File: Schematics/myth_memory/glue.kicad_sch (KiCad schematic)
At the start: 6 parts, among them U1 74HC04, U12 74LS32, U4 74LS32, U5 74LS21, U6 4002, U8 4075

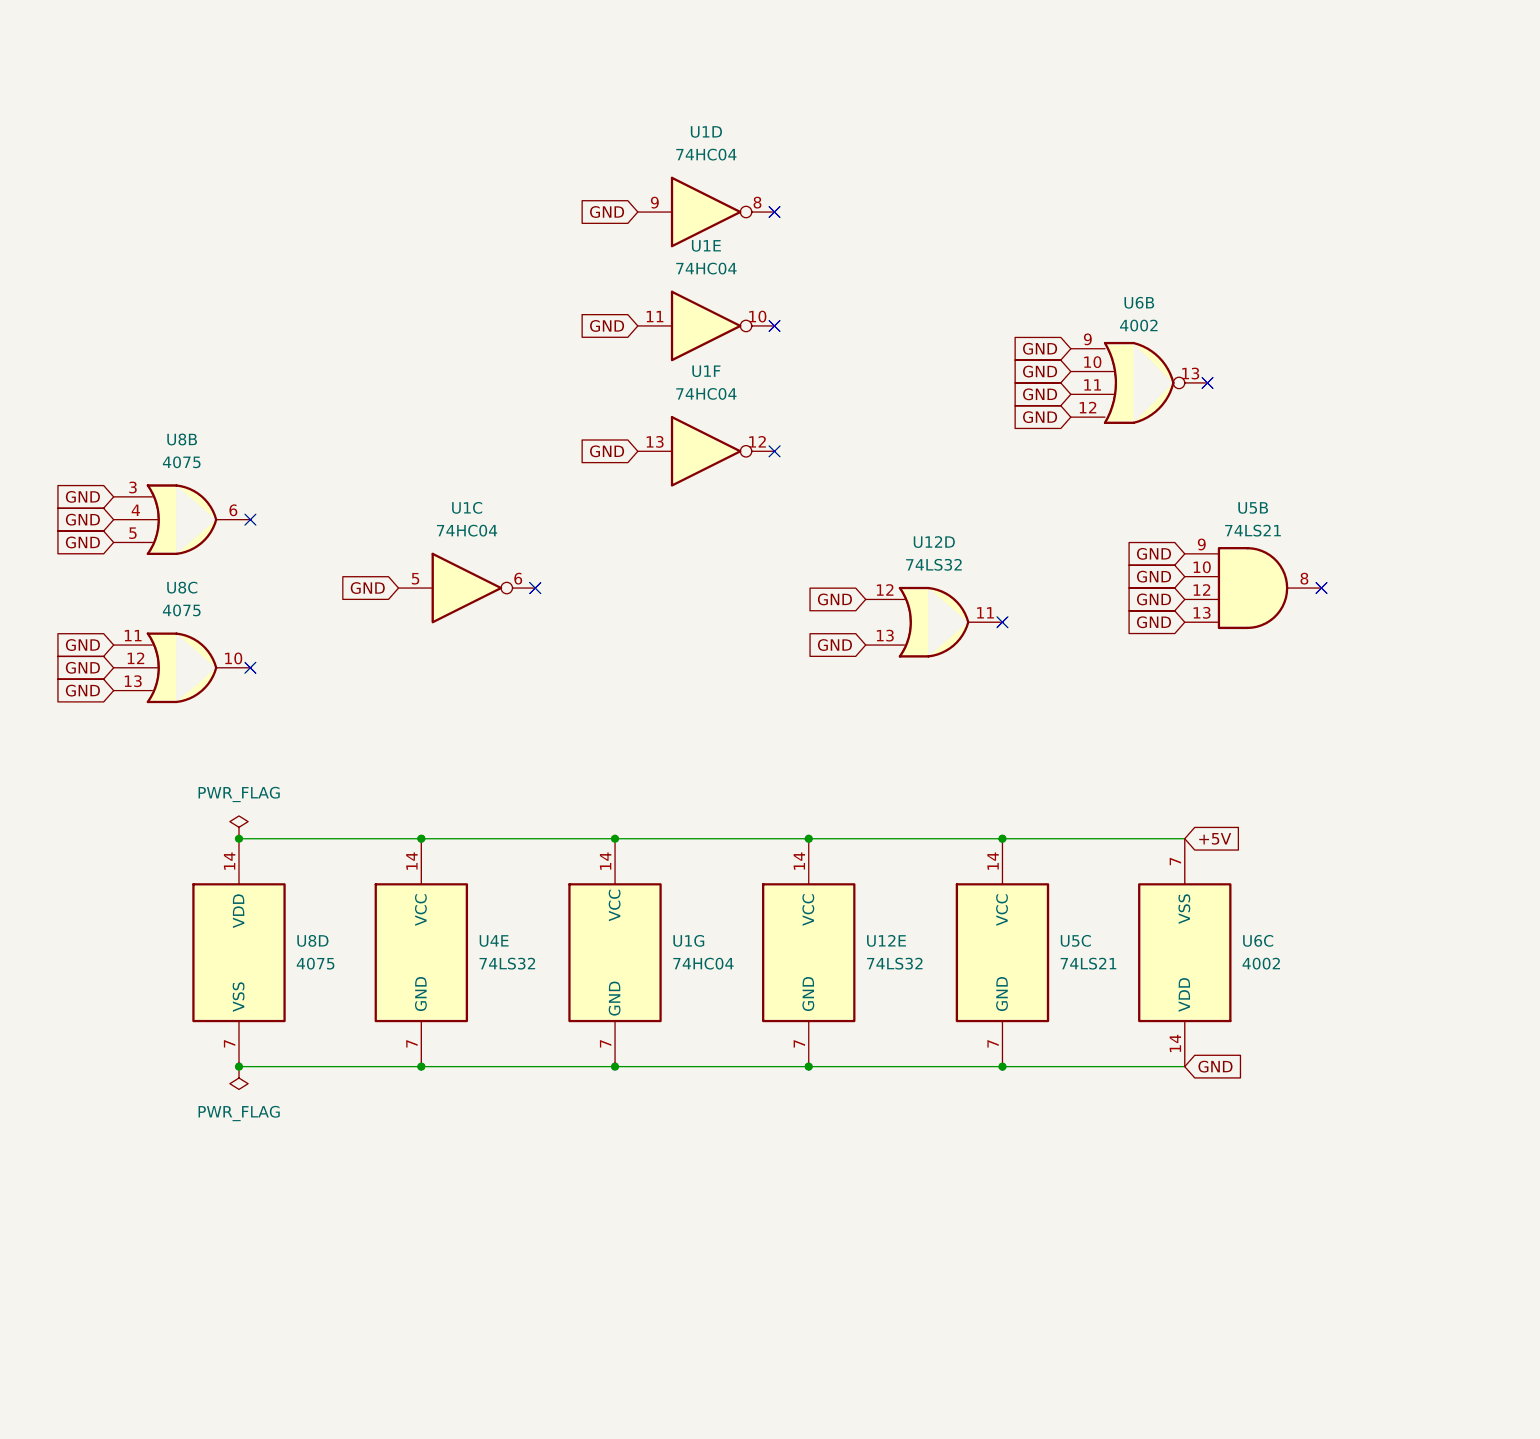
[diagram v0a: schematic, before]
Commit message: Change d to g
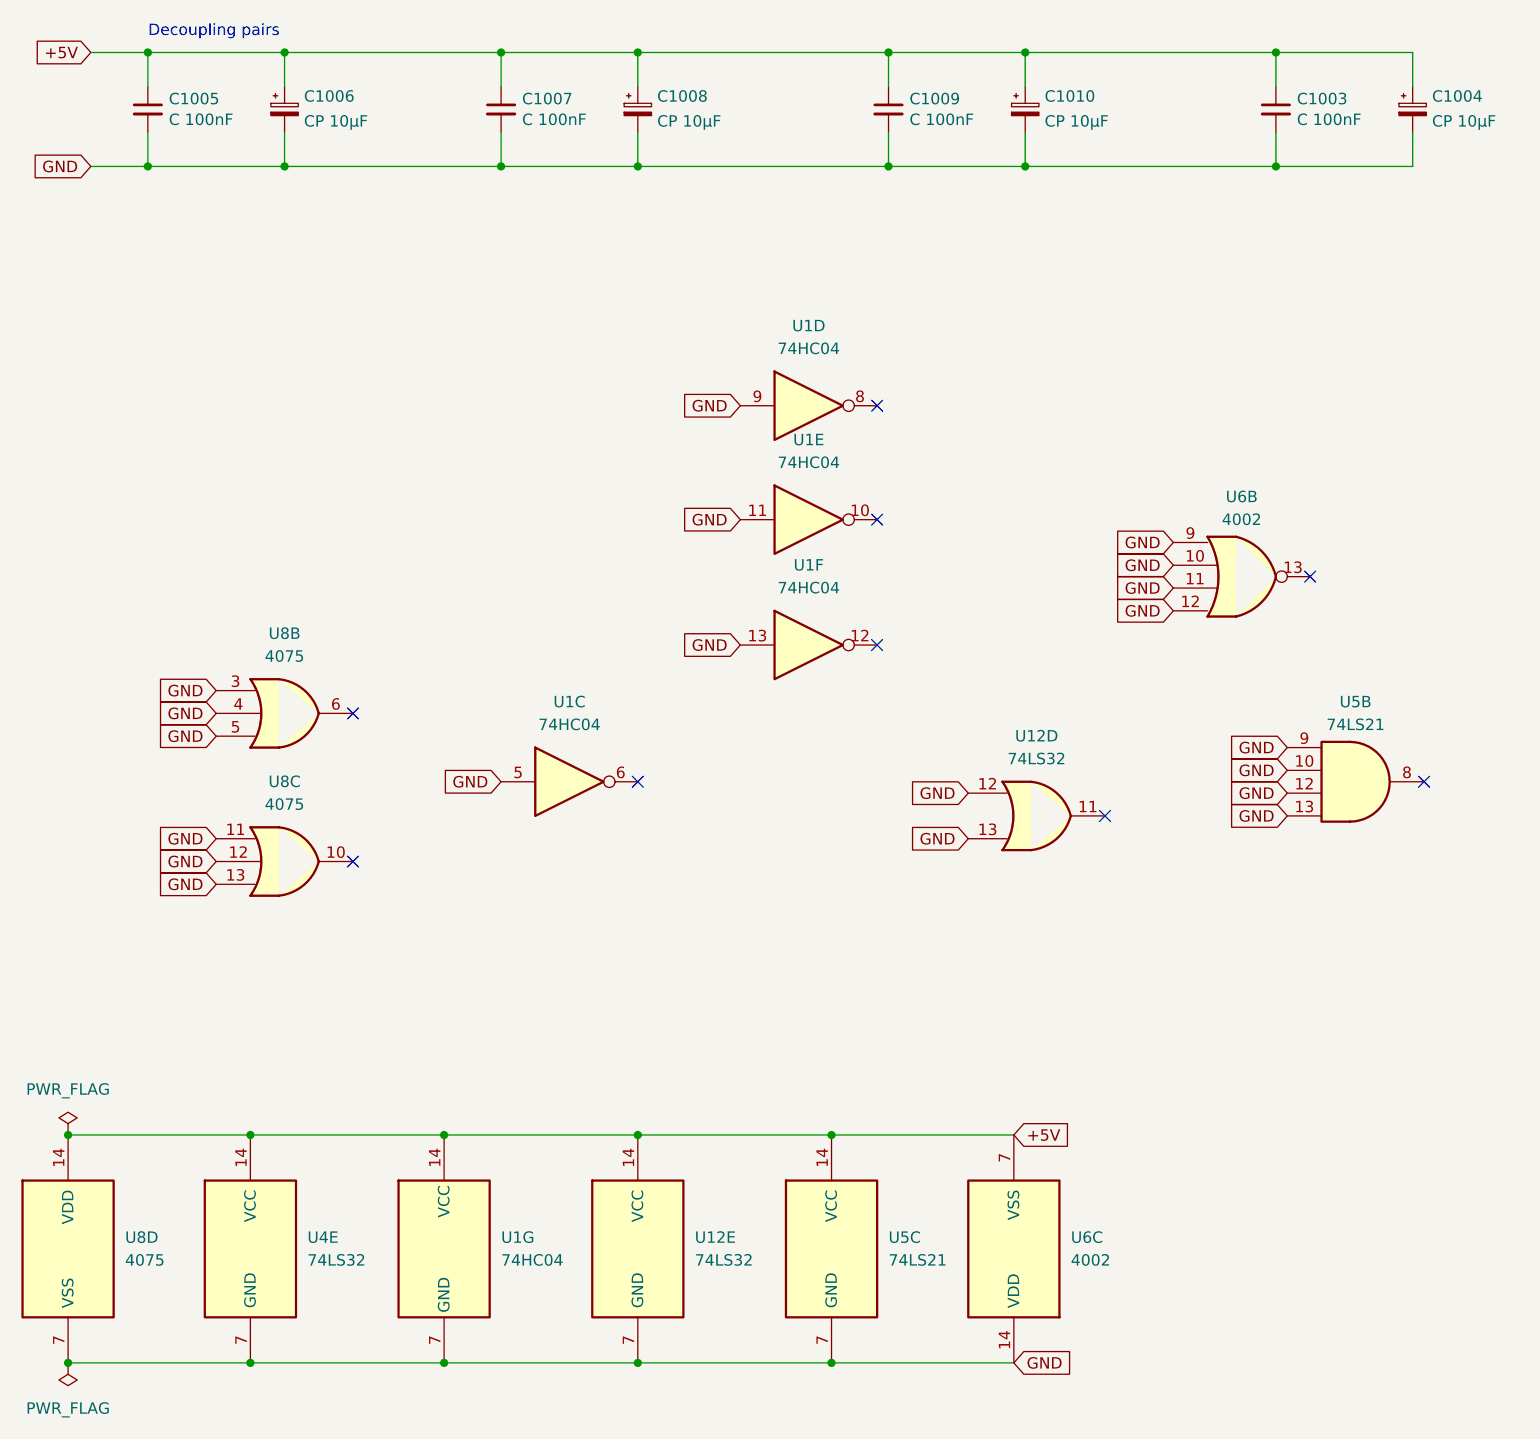
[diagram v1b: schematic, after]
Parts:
- added C1003, C1005, C1007, C1009: C 100nF, Capacitor_THT:C_Disc_D5.0mm_W2.5mm_P2.50mm, symbol Device:C_Small
- added C1004, C1006, C1008, C1010: CP 10μF, Capacitor_THT:CP_Radial_D6.3mm_P2.50mm, symbol Device:C_Polarized_Small
- U1, U12, U4, U5, U6, U8: footprint (none) -> Package_DIP:DIP-14_W7.62mm_LongPads
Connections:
- net +5V: now also C1003.1, C1004.1, C1005.1, C1006.1, C1007.1, C1008.1, C1009.1, C1010.1
- net GND: now also C1003.2, C1004.2, C1005.2, C1006.2, C1007.2, C1008.2, C1009.2, C1010.2
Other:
- note added: "Decoupling pairs"
- moved on the sheet: U12D, U12E, U1C, U1D, U1E, U1F, U1G, U4E, U5B, U5C, U6B, U6C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
